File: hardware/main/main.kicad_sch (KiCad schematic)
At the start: 28 parts, among them J101 ST_LINK, J102 USART

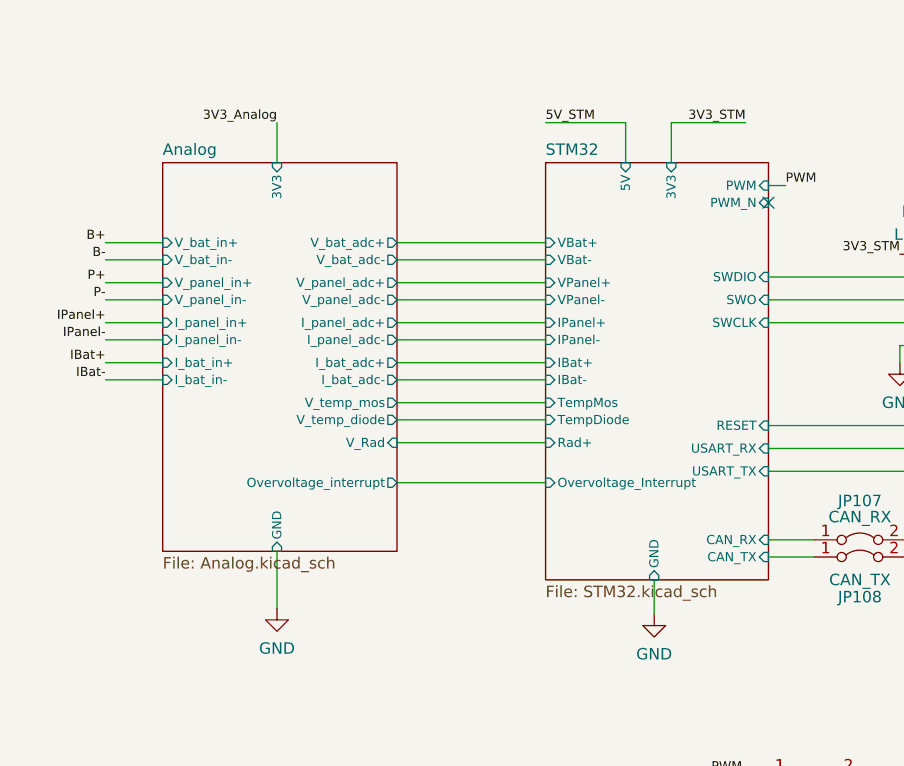
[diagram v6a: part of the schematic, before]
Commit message: Schematics: Add STM32 comparator for Battery OverVoltage
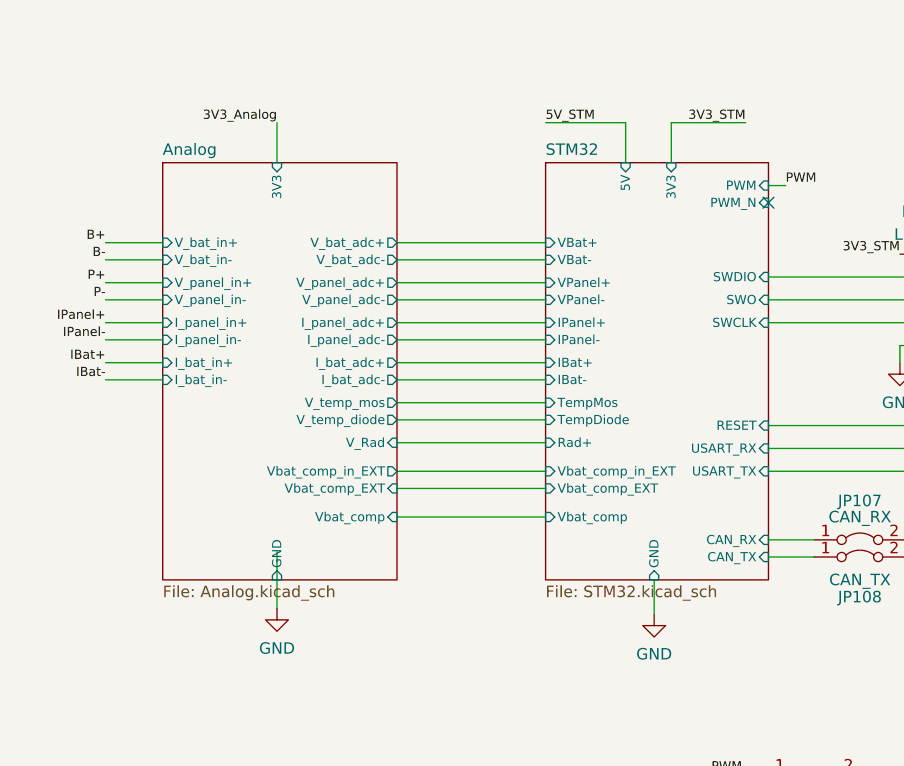
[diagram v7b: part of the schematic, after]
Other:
- sheet Analog ports: added Vbat_comp, Vbat_comp_EXT, Vbat_comp_in_EXT; removed Overvoltage_interrupt
- sheet STM32 ports: added Vbat_comp, Vbat_comp_EXT, Vbat_comp_in_EXT; removed Overvoltage_Interrupt
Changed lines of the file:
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@@
+    (stroke (width 0) (type default) (color 0 0 0 0))
+  )
+  (wire (pts (xy 114.935 80.645) (xy 131.445 80.645))
     (stroke (width 0) (type default) (color 0 0 0 0))
   )
@@
     (stroke (width 0) (type default) (color 0 0 0 0))
   )
+  (wire (pts (xy 114.935 78.74) (xy 131.445 78.74))
+    (stroke (width 0) (type default) (color 0 0 0 0))
+  )
   (wire (pts (xy 161.29 151.765) (xy 168.91 151.765))
     (stroke (width 0) (type default) (color 0 0 0 0))
@@
     (stroke (width 0) (type default) (color 0 0 0 0))
   )
-  (wire (pts (xy 114.935 80.01) (xy 131.445 80.01))
+  (wire (pts (xy 114.935 83.82) (xy 131.445 83.82))
     (stroke (width 0) (type default) (color 0 0 0 0))
   )
@@
     (pin "4")
   )
-  (sheet (at 88.9 44.45) (size 26.035 43.18) (fields_autoplaced)
+  (sheet (at 88.9 44.45) (size 26.035 46.355) (fields_autoplaced)
     (stroke (width 0.1524) (type solid) (color 0 0 0 0))
     (fill (color 0 0 0 0.0000))
@@
       (effects (font (size 1.27 1.27)) (justify left bottom))
     )
-    (property "Sheet file" "Analog.kicad_sch" (id 1) (at 88.9 88.2146 0)
+    (property "Sheet file" "Analog.kicad_sch" (id 1) (at 88.9 91.3896 0)
       (effects (font (size 1.27 1.27)) (justify left top))
     )
@@
       (effects (font (size 1.016 1.016)) (justify left))
     )
-    (pin "Overvoltage_interrupt" output (at 114.935 80.01 0)
-      (effects (font (size 1.016 1.016)) (justify right))
-    )
     (pin "I_panel_in+" input (at 88.9 62.23 180)
       (effects (font (size 1.016 1.016)) (justify left))
@@
       (effects (font (size 1.016 1.016)) (justify right))
     )
-    (pin "GND" input (at 101.6 87.63 270)
+    (pin "GND" input (at 101.6 90.805 270)
       (effects (font (size 1.016 1.016)) (justify left))
     )
@@
     )
     (pin "V_Rad" input (at 114.935 75.565 0)
+      (effects (font (size 1.016 1.016)) (justify right))
+    )
+    (pin "Vbat_comp_in_EXT" output (at 114.935 78.74 0)
+      (effects (font (size 1.016 1.016)) (justify right))
+    )
+    (pin "Vbat_comp_EXT" input (at 114.935 80.645 0)
+      (effects (font (size 1.016 1.016)) (justify right))
+    )
+    (pin "Vbat_comp" input (at 114.935 83.82 0)
       (effects (font (size 1.016 1.016)) (justify right))
     )
@@
       (effects (font (size 1.016 1.016)) (justify right))
     )
-    (pin "Overvoltage_Interrupt" input (at 131.445 80.01 180)
+    (pin "Vbat_comp_EXT" input (at 131.445 80.645 180)
+      (effects (font (size 1.016 1.016)) (justify left))
+    )
+    (pin "Vbat_comp_in_EXT" input (at 131.445 78.74 180)
+      (effects (font (size 1.016 1.016)) (justify left))
+    )
+    (pin "Vbat_comp" input (at 131.445 83.82 180)
       (effects (font (size 1.016 1.016)) (justify left))
     )
@@
       (reference "#PWR0112") (unit 1) (value "GND") (footprint "")
     )
+    (path "/d443602e-c945-466d-a5b3-f4f57ead3f21/61e88691-4a6e-444a-a8fa-6fc4ea4d57b1"
+      (reference "#PWR0113") (unit 1) (value "GND") (footprint "")
+    )
+    (path "/d443602e-c945-466d-a5b3-f4f57ead3f21/e71e4456-9d41-4c00-96dd-c784b5611e57"
+      (reference "#PWR0114") (unit 1) (value "GND") (footprint "")
+    )
+    (path "/5ce5fb2d-189a-4c71-a5ce-76d878c8bc18/56285478-ef89-4a57-8eee-d03c1823e4af"
+      (reference "#PWR0115") (unit 1) (value "GNDA") (footprint "")
+    )
+    (path "/5ce5fb2d-189a-4c71-a5ce-76d878c8bc18/b8f61f9c-06c1-40f9-a89c-349de5c5cc92"
+      (reference "#PWR0116") (unit 1) (value "GNDA") (footprint "")
+    )
+    (path "/5ce5fb2d-189a-4c71-a5ce-76d878c8bc18/32b45182-94f3-46b1-a424-4585413dda44"
+      (reference "#PWR0117") (unit 1) (value "GNDA") (footprint "")
+    )
+    (path "/5ce5fb2d-189a-4c71-a5ce-76d878c8bc18/193f2fa2-4963-436f-990a-eb724d6883da"
+      (reference "#PWR0118") (unit 1) (value "GNDA") (footprint "")
+    )
     (path "/d443602e-c945-466d-a5b3-f4f57ead3f21/f63aed26-bfdb-469b-a9f7-d886bb8f3b52"
       (reference "#PWR0201") (unit 1) (value "GND") (footprint "")
@@
       (reference "D204") (unit 1) (value "LED_0") (footprint "LED_SMD:LED_0805_2012Metric_Pad1.15x1.40mm_HandSolder")
     )
+    (path "/d443602e-c945-466d-a5b3-f4f57ead3f21/9d41b42a-b039-4a35-b044-6eaa920c116d"
+      (reference "D205") (unit 1) (value "Bat_OverV_Out") (footprint "LED_SMD:LED_0805_2012Metric_Pad1.15x1.40mm_HandSolder")
+    )
     (path "/5ce5fb2d-189a-4c71-a5ce-76d878c8bc18/9fb4c33f-5a45-4a3c-b901-c82d2e05eb1e"
       (reference "D301") (unit 1) (value "ESD351DPYR") (footprint "Diode_SMD:D_0402_1005Metric_Pad0.77x0.64mm_HandSolder")
@@
       (reference "JP203") (unit 1) (value "Analog_Ref") (footprint "Jumper:SolderJumper-3_P1.3mm_Open_Pad1.0x1.5mm")
     )
+    (path "/d443602e-c945-466d-a5b3-f4f57ead3f21/d59251c6-1dcd-4e74-a7b4-a29ca8ce84e2"
+      (reference "JP204") (unit 1) (value "ID_0") (footprint "Jumper:SolderJumper-2_P1.3mm_Open_TrianglePad1.0x1.5mm")
+    )
+    (path "/d443602e-c945-466d-a5b3-f4f57ead3f21/d01ef1c7-343d-4cfd-9c79-3a2f939a02f8"
+      (reference "JP205") (unit 1) (value "ID_1") (footprint "Jumper:SolderJumper-2_P1.3mm_Open_TrianglePad1.0x1.5mm")
+    )
+    (path "/d443602e-c945-466d-a5b3-f4f57ead3f21/d16577f1-cd45-4bb8-8c16-60f0259d54c7"
+      (reference "JP206") (unit 1) (value "ID_2") (footprint "Jumper:SolderJumper-2_P1.3mm_Open_TrianglePad1.0x1.5mm")
+    )
+    (path "/d443602e-c945-466d-a5b3-f4f57ead3f21/37b23684-4d2c-4def-8636-74742085388a"
+      (reference "JP207") (unit 1) (value "ID_3") (footprint "Jumper:SolderJumper-2_P1.3mm_Open_TrianglePad1.0x1.5mm")
+    )
     (path "/5ce5fb2d-189a-4c71-a5ce-76d878c8bc18/92078646-f255-459b-b626-986c8ba27a42"
       (reference "JP301") (unit 1) (value "Disable_Vpanel") (footprint "Jumper:SolderJumper-2_P1.3mm_Open_TrianglePad1.0x1.5mm")
@@
       (reference "R207") (unit 1) (value "1kR 0805") (footprint "Resistor_SMD:R_0805_2012Metric_Pad1.20x1.40mm_HandSolder")
     )
+    (path "/d443602e-c945-466d-a5b3-f4f57ead3f21/fb01cb78-13f6-4e1c-a8f6-1082a37aef82"
+      (reference "R208") (unit 1) (value "1kR 0805") (footprint "Resistor_SMD:R_0805_2012Metric_Pad1.20x1.40mm_HandSolder")
+    )
     (path "/5ce5fb2d-189a-4c71-a5ce-76d878c8bc18/9142cd31-94d5-46bd-8f1e-498b2062c730"
       (reference "R301") (unit 1) (value "?") (footprint "Resistor_SMD:R_0805_2012Metric_Pad1.20x1.40mm_HandSolder")
@@
       (reference "R321") (unit 1) (value "100R 0805") (footprint "Resistor_SMD:R_0805_2012Metric_Pad1.20x1.40mm_HandSolder")
     )
+    (path "/5ce5fb2d-189a-4c71-a5ce-76d878c8bc18/e04de51b-7a24-4839-a652-c84e2402b9e3"
+      (reference "R322") (unit 1) (value "NC") (footprint "Resistor_SMD:R_0805_2012Metric_Pad1.20x1.40mm_HandSolder")
+    )
+    (path "/5ce5fb2d-189a-4c71-a5ce-76d878c8bc18/278a9185-bcf1-42ed-9194-e75ece3bd37b"
+      (reference "R323") (unit 1) (value "NC") (footprint "Resistor_SMD:R_0805_2012Metric_Pad1.20x1.40mm_HandSolder")
+    )
+    (path "/5ce5fb2d-189a-4c71-a5ce-76d878c8bc18/ff196370-2d0d-40c4-baee-bd5a0a8427ee"
+      (reference "R324") (unit 1) (value "?") (footprint "Resistor_SMD:R_0805_2012Metric_Pad1.20x1.40mm_HandSolder")
+    )
+    (path "/5ce5fb2d-189a-4c71-a5ce-76d878c8bc18/60cc7f1e-b16e-4ed0-b6c7-dda10aedeed5"
+      (reference "R325") (unit 1) (value "?") (footprint "Resistor_SMD:R_0805_2012Metric_Pad1.20x1.40mm_HandSolder")
+    )
     (path "/9e3280d3-dce3-416e-a0bb-0596067104fa/120151ea-e52d-46e5-9db6-e4d83014dbca"
       (reference "R402") (unit 1) (value "2W 200V 10R ±5% 2512") (footprint "Resistor_SMD:R_2512_6332Metric_Pad1.40x3.35mm_HandSolder")
@@
       (reference "TP202") (unit 1) (value "DB_1") (footprint "TestPoint:TestPoint_Pad_2.0x2.0mm")
     )
+    (path "/d443602e-c945-466d-a5b3-f4f57ead3f21/6688947b-9ff9-46d3-8692-70446d611d3a"
+      (reference "TP203") (unit 1) (value "Timer_Break") (footprint "TestPoint:TestPoint_Pad_2.0x2.0mm")
+    )
     (path "/d443602e-c945-466d-a5b3-f4f57ead3f21/b6040504-a017-4434-a4ba-a1ed179eebcc"

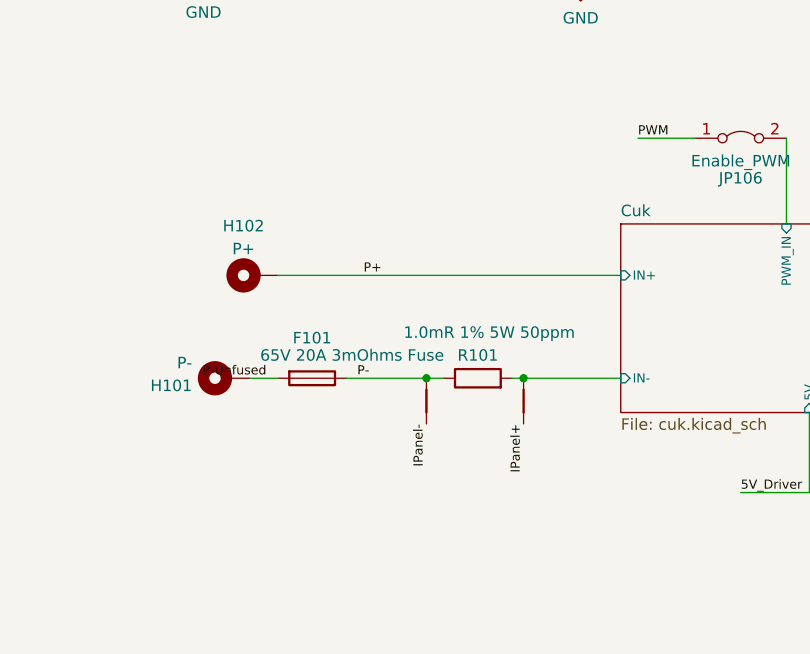
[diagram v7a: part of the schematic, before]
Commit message: Layout: Fist version of power stage
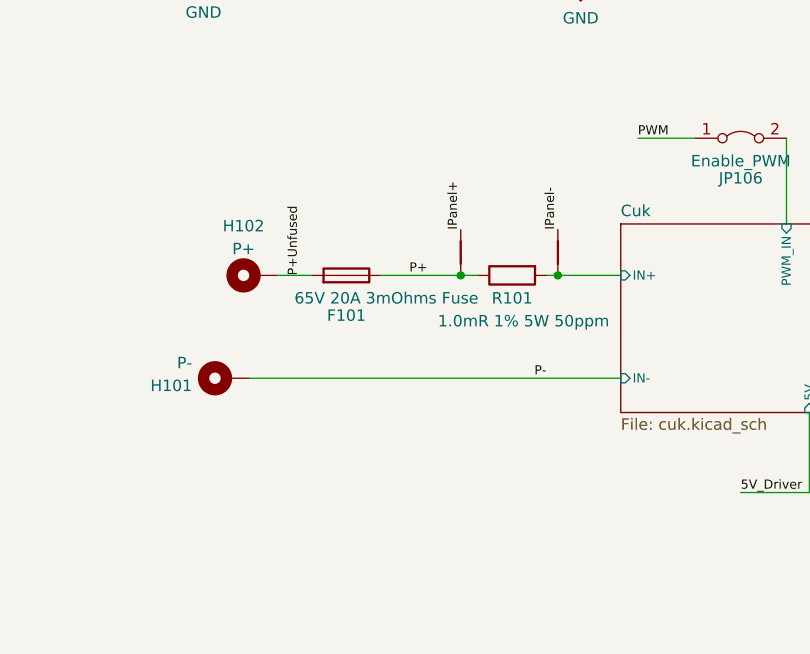
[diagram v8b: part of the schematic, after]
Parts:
- JP101, JP102, JP103, JP104, JP105, JP106, JP107, JP108, JP109, JP110: footprint Jumper:SolderJumper-2_P1.3mm_Open_TrianglePad1.0x1.5mm -> Zenite:SolderJumper-2_P0.5mm_Open_TrianglePad0.5x0.5mm
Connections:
- net IPanel+: now also NT101.1; no longer NT102.1
- net IPanel-: now also NT102.1; no longer NT101.1
- net P+: now also F101.1, NT101.2, R101.1; no longer H102.1
- net P-: now also H101.1; no longer F101.1, NT101.2, R101.1
- net Cuk/IN- renamed Cuk/IN+
- net P-Unfused renamed P+Unfused
- net P+Unfused: now also H102.1; no longer H101.1
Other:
- moved on the sheet: F101, R101
